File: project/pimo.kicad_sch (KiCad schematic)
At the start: 8 parts, among them J1 RPi_GPIO, J11 Conn_01x03_Pin, U1 W25Q32JVSS

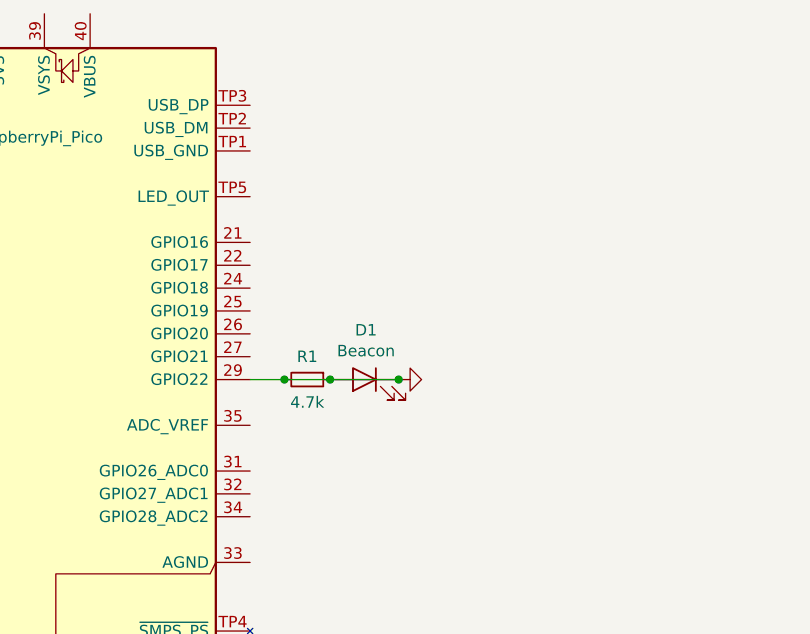
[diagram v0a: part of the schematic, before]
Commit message: pmod added.
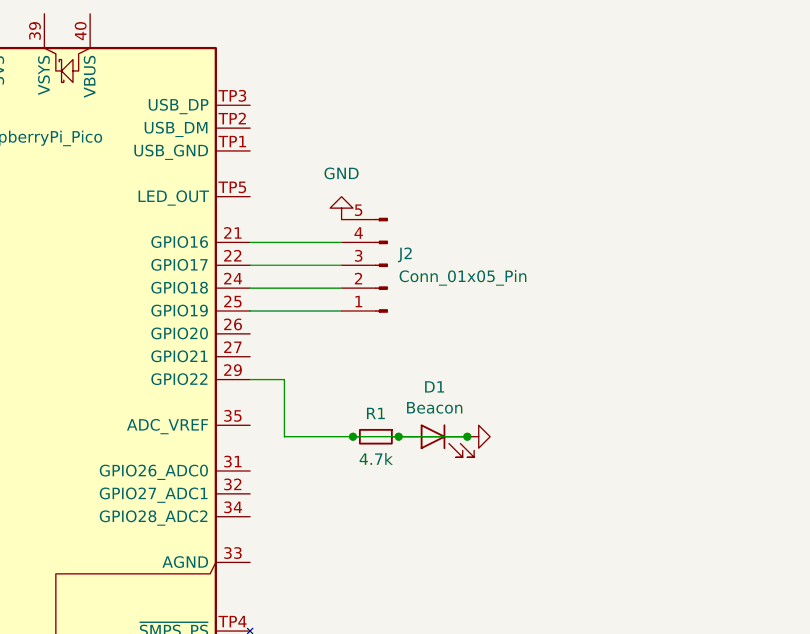
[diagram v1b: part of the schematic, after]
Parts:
- added J2: Conn_01x05_Pin, symbol Connector:Conn_01x05_Pin
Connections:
- net GND: now also J2.5 (Pin_5)
- net at A1.21 (GPIO16): now also J2.4 (Pin_4)
- net at A1.22 (GPIO17): now also J2.3 (Pin_3)
- net at A1.24 (GPIO18): now also J2.2 (Pin_2)
- net at A1.25 (GPIO19): now also J2.1 (Pin_1)
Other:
- moved on the sheet: D1, R1
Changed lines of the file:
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@@
 	)
 	(junction
-		(at 106.68 86.36)
+		(at 119.38 92.71)
 		(diameter 0)
 		(color 0 0 0 0)
 	)
 	(junction
-		(at 111.76 86.36)
+		(at 114.3 92.71)
 		(diameter 0)
 		(color 0 0 0 0)
@@
 	)
 	(junction
-		(at 119.38 86.36)
+		(at 127 92.71)
 		(diameter 0)
 		(color 0 0 0 0)
@@
 	(wire
 		(pts
+			(xy 102.87 76.2) (xy 113.03 76.2)
+		)
+		(stroke
+			(width 0)
+			(type default)
+		)
+	)
+	(wire
+		(pts
 			(xy 152.4 165.1) (xy 156.21 165.1)
 		)
@@
 		)
 	)
+	(wire
+		(pts
+			(xy 106.68 86.36) (xy 106.68 92.71)
+		)
+		(stroke
+			(width 0)
+			(type default)
+		)
+	)
 	(bus
 		(pts
@@
 	(wire
 		(pts
-			(xy 111.76 86.36) (xy 106.68 86.36)
+			(xy 119.38 92.71) (xy 114.3 92.71)
+		)
+		(stroke
+			(width 0)
+			(type default)
+		)
+	)
+	(wire
+		(pts
+			(xy 106.68 92.71) (xy 114.3 92.71)
 		)
 		(stroke
@@
 		)
 	)
+	(wire
+		(pts
+			(xy 102.87 73.66) (xy 113.03 73.66)
+		)
+		(stroke
+			(width 0)
+			(type default)
+		)
+	)
 	(bus
 		(pts
@@
 		)
 	)
+	(wire
+		(pts
+			(xy 102.87 78.74) (xy 113.03 78.74)
+		)
+		(stroke
+			(width 0)
+			(type default)
+		)
+	)
 	(bus
 		(pts
@@
 	(wire
 		(pts
-			(xy 119.38 86.36) (xy 111.76 86.36)
+			(xy 127 92.71) (xy 119.38 92.71)
 		)
 		(stroke
@@
 		(pts
 			(xy 101.6 170.18) (xy 101.6 172.72)
+		)
+		(stroke
+			(width 0)
+			(type default)
+		)
+	)
+	(wire
+		(pts
+			(xy 102.87 71.12) (xy 113.03 71.12)
 		)
 		(stroke
@@
 	(symbol
 		(lib_id "Device:LED")
-		(at 115.57 86.36 0)
+		(at 123.19 92.71 0)
 		(mirror y)
 		(unit 1)
@@
 		(dnp no)
 		(property "Reference" "D1"
-			(at 115.7478 80.8736 0)
+			(at 123.3678 87.2236 0)
 			(effects
 				(font
@@
 		)
 		(property "Value" "Beacon"
-			(at 115.7478 83.185 0)
+			(at 123.3678 89.535 0)
 			(effects
 				(font
@@
 		)
 		(property "Footprint" "LED_SMD:LED_0603_1608Metric"
-			(at 115.57 86.36 0)
+			(at 123.19 92.71 0)
 			(effects
 				(font
@@
 		)
 		(property "Datasheet" "~"
-			(at 115.57 86.36 0)
+			(at 123.19 92.71 0)
 			(effects
 				(font
@@
 		)
 		(property "Description" ""
-			(at 115.57 86.36 0)
+			(at 123.19 92.71 0)
 			(effects
 				(font
@@
 	(symbol
 		(lib_id "Device:R_Small")
-		(at 109.22 86.36 270)
+		(at 116.84 92.71 270)
 		(unit 1)
 		(exclude_from_sim no)
@@
 		(dnp no)
 		(property "Reference" "R1"
-			(at 109.22 83.82 90)
+			(at 116.84 90.17 90)
 			(effects
 				(font
@@
 		)
 		(property "Value" "4.7k"
-			(at 109.22 88.9 90)
+			(at 116.84 95.25 90)
 			(effects
 				(font
@@
 		)
 		(property "Footprint" "Resistor_SMD:R_0603_1608Metric"
-			(at 109.22 86.36 0)
+			(at 116.84 92.71 0)
 			(effects
 				(font
@@
 		)
 		(property "Datasheet" "~"
-			(at 109.22 86.36 0)
+			(at 116.84 92.71 0)
 			(effects
 				(font
@@
 		)
 		(property "Description" ""
-			(at 109.22 86.36 0)
+			(at 116.84 92.71 0)
 			(effects
 				(font
@@
 	(symbol
 		(lib_id "power:GND")
-		(at 119.38 86.36 90)
+		(at 127 92.71 90)
 		(mirror x)
 		(unit 1)
@@
 		(dnp no)
 		(property "Reference" "#PWR015"
-			(at 125.73 86.36 0)
+			(at 133.35 92.71 0)
 			(effects
 				(font
@@
 		)
 		(property "Value" "GND"
-			(at 123.7742 86.487 0)
+			(at 131.3942 92.837 0)
 			(effects
 				(font
@@
 		)
 		(property "Footprint" ""
-			(at 119.38 86.36 0)
+			(at 127 92.71 0)
 			(effects
 				(font
@@
 		)
 		(property "Datasheet" ""
-			(at 119.38 86.36 0)
+			(at 127 92.71 0)
 			(effects
 				(font
@@
 		)
 		(property "Description" ""
-			(at 119.38 86.36 0)
+			(at 127 92.71 0)
 			(effects
 				(font
@@
 	(symbol
 		(lib_id "power:GND")
+		(at 113.03 68.58 180)
+		(unit 1)
+		(exclude_from_sim no)
+		(in_bom yes)
+		(on_board yes)
+		(dnp no)
+		(fields_autoplaced yes)
+		(property "Reference" "#PWR2"
+			(at 113.03 62.23 0)
+			(effects
+				(font
+					(size 1.27 1.27)
+				)
+				(hide yes)
+			)
+		)
+		(property "Value" "GND"
+			(at 113.03 63.5 0)
+			(effects
+				(font
+					(size 1.27 1.27)
+				)
+			)
+		)
+		(property "Footprint" ""
+			(at 113.03 68.58 0)
+			(effects
+				(font
+					(size 1.27 1.27)
+				)
+				(hide yes)
+			)
+		)
+		(property "Datasheet" ""
+			(at 113.03 68.58 0)
+			(effects
+				(font
+					(size 1.27 1.27)
+				)
+				(hide yes)
+			)
+		)
+		(property "Description" "Power symbol creates a global label with name \"GND\" , ground"
+			(at 113.03 68.58 0)
+			(effects
+				(font
+					(size 1.27 1.27)
+				)
+				(hide yes)
+			)
+		)
+		(pin "1"
+		)
+		(instances
+			(project ""
+				(path "/3f830ea6-5a5f-4b7b-8d42-0620c39d4ee6"
+					(reference "#PWR2")
+					(unit 1)
+				)
+			)
+		)
+	)
+	(symbol
+		(lib_id "power:GND")
 		(at 193.04 69.85 270)
 		(unit 1)
@@
 					(unit 1)
 				)
+			)
+		)
+	)
+	(symbol
+		(lib_id "Connector:Conn_01x05_Pin")
+		(at 118.11 73.66 180)
+		(unit 1)
+		(exclude_from_sim no)
+		(in_bom yes)
+		(on_board yes)
+		(dnp no)
+		(fields_autoplaced yes)
+		(property "Reference" "J2"
+			(at 119.38 72.3899 0)
+			(effects
+				(font
+					(size 1.27 1.27)
+				)
+				(justify right)
+			)
+		)
+		(property "Value" "Conn_01x05_Pin"
+			(at 119.38 74.9299 0)
+			(effects
+				(font
+					(size 1.27 1.27)
+				)
+				(justify right)
+			)
+		)
+		(property "Footprint" ""
+			(at 118.11 73.66 0)
+			(effects
+				(font
+					(size 1.27 1.27)
+				)
+				(hide yes)
+			)
+		)
+		(property "Datasheet" "~"
+			(at 118.11 73.66 0)
+			(effects
+				(font
+					(size 1.27 1.27)
+				)
+				(hide yes)
+			)
+		)
+		(property "Description" "Generic connector, single row, 01x05, script generated"
+			(at 118.11 73.66 0)
+			(effects
+				(font
+					(size 1.27 1.27)
+				)
+				(hide yes)
+			)
+		)
+		(pin "3"
+		)
+		(pin "5"
+		)
+		(pin "2"
+		)
+		(pin "4"
+		)
+		(pin "1"
+		)
+		(instances
+			(project ""
+				(path "/3f830ea6-5a5f-4b7b-8d42-0620c39d4ee6"
+					(reference "J2")
+					(unit 1)
+				)

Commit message: jtag symbol added
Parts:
- added J3: Conn_ARM_JTAG_SWD_10, symbol Connector:Conn_ARM_JTAG_SWD_10
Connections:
- net TCK renamed SWCLK/TCK
- net TDI renamed NC/TDI
- net TDO renamed SWO/TDO
- net TMS renamed SWDIO/TMS
- net TRST renamed RESET
- new net: J3.3 (GND), J3.5 (GND)
